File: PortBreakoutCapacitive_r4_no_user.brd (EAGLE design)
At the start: 24.4 x 49.8 mm, 10 parts, among them IC1 AT42QT1011-TSHR

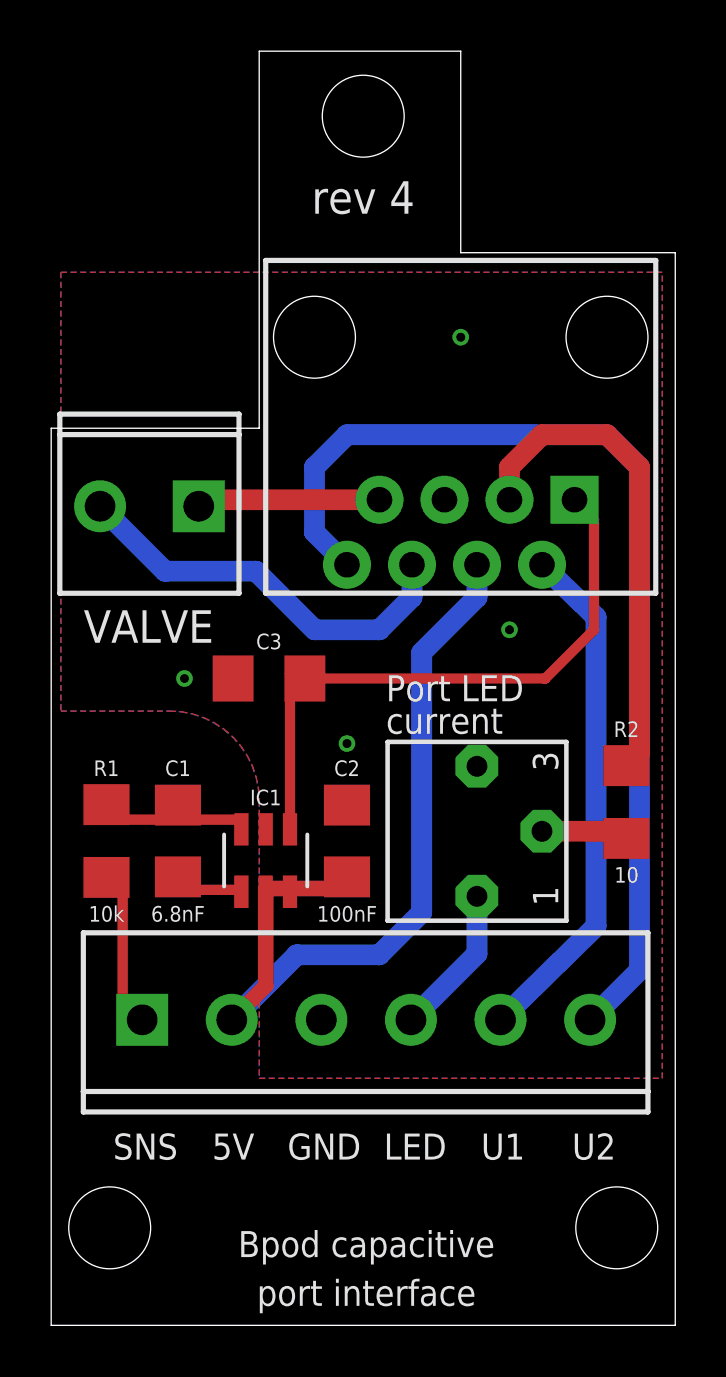
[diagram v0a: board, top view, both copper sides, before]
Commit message: rev 4: C1 with lower capacitance
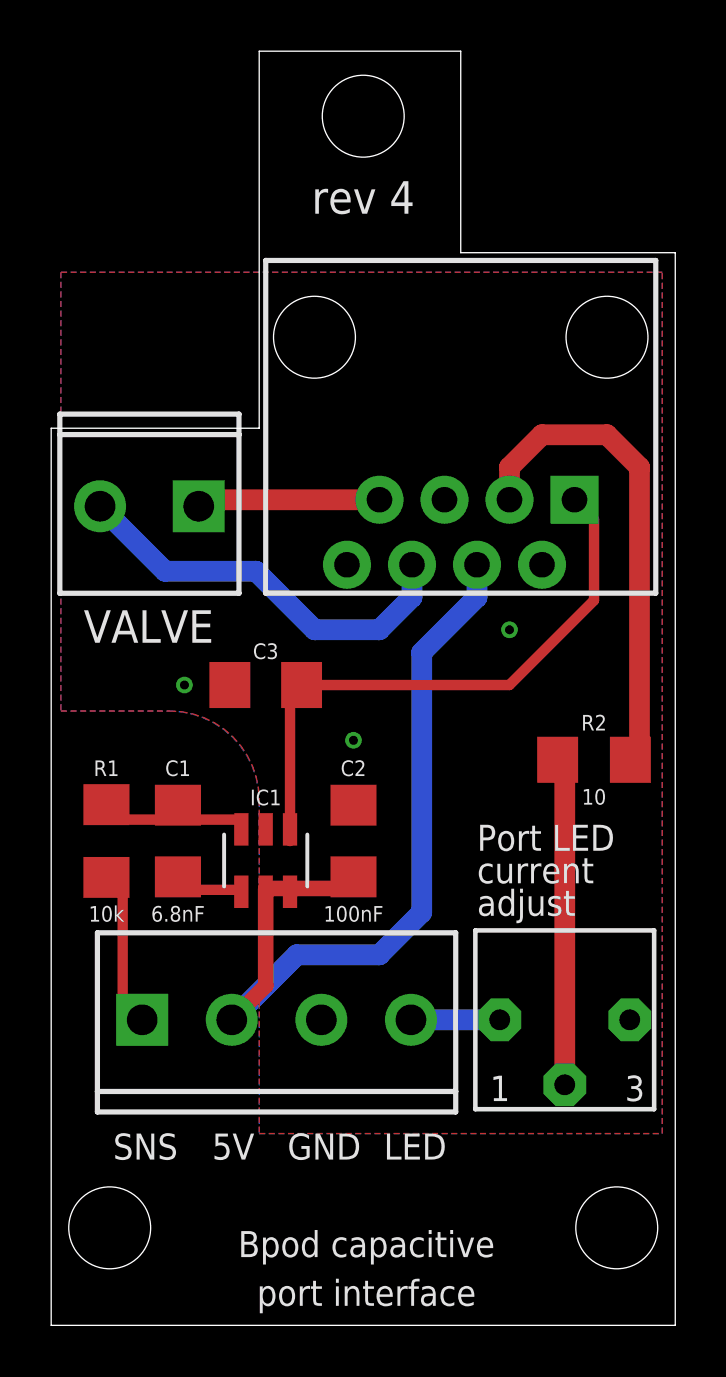
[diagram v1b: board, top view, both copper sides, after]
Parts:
- JP1: device SparkFun:SCREWTERMINAL-3.5MM-6 -> SparkFun-Connectors:SCREWTERMINAL-3.5MM-4
- moved R3 8.13 mm to (21.2, 12.7), turned to 0 degrees
- moved R2 2.08 mm to (22.4, 22.9), turned to 0 degrees
- moved C3 0.28 mm to (9.53, 25.8), turned to 180 degrees
- moved C2 0.25 mm to (13.0, 19.7)
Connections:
- removed net SENSOR: C3.2, IC1.1, U$1.1
- removed net USER1: JP1.5, U$1.2
- removed net USER2: JP1.6, U$1.8
- new net OUT: C3.1, IC1.1, U$1.1
- net GND: now also C3.2; no longer C3.1
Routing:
- net USER2: track 40.5 -> 0.00 mm
- net SENSOR: track 24.2 -> 0.00 mm
- net OUT: track 0.00 -> 23.5 mm
- net USER1: track 20.2 -> 0.00 mm
- net N$4: track 3.42 -> 12.9 mm
- net N$7: track 5.90 -> 3.47 mm
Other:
- board text added: "adjust"
- board text removed: "U1"
- board text removed: "U2"

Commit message: some changes to trace routing
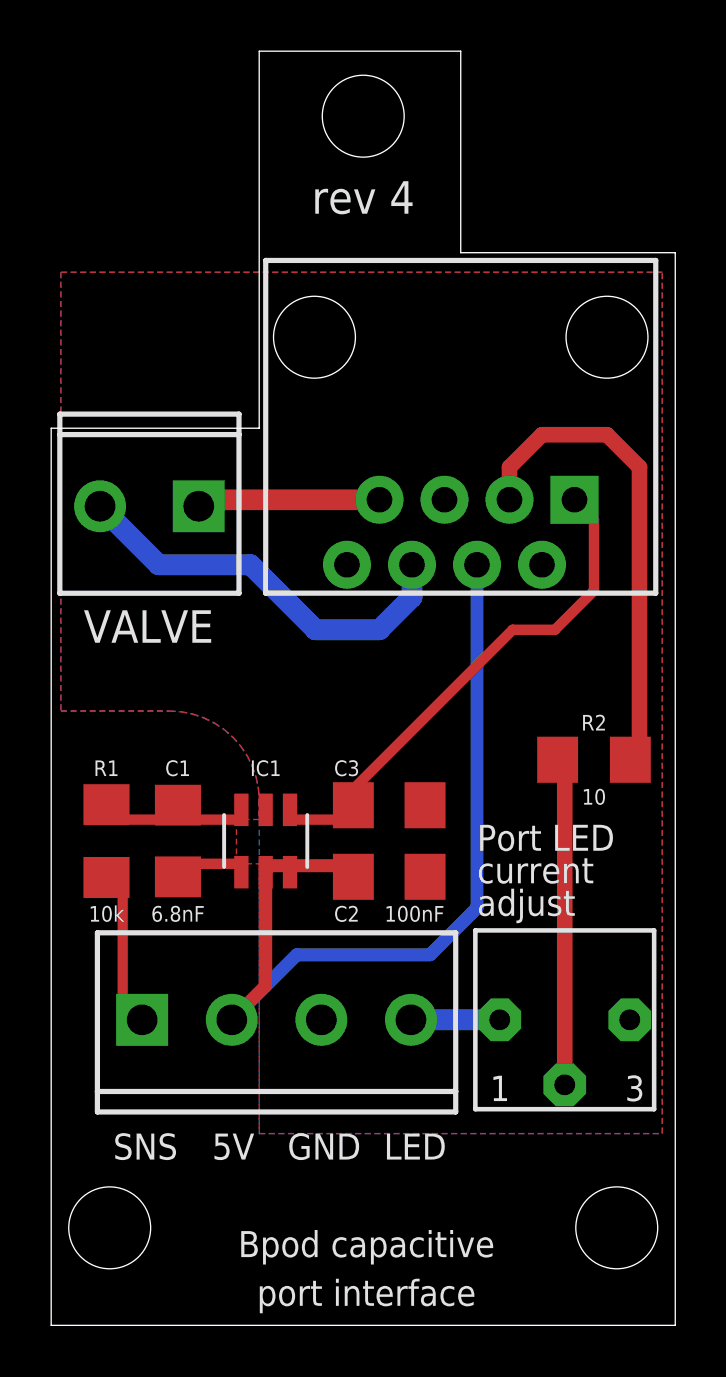
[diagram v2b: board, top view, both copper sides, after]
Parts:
- moved C3 6.74 mm to (14.4, 21.1), turned to 0 degrees
- moved C2 1.98 mm to (14.4, 18.3), turned to 0 degrees
- moved IC1 0.76 mm to (9.53, 19.7)
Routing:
- net OUT: track 23.5 -> 20.2 mm
- net VCC: track 33.1 -> 35.5 mm
